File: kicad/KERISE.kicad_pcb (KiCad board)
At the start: 2 copper layers, 49 x 50 mm, 128 parts, among them J1 COM, J10 Ref_Slave, J11 Ref_Host, J12 Ref_Slave, J13 Ref_Host, J14 Ref_Slave, J15 Motor_L, J16 Motor_R, J17 5077CR-16-SMC2-BK-TR, J18 COM, J19 Charge1, J2 ENC_Host, J20 Charge2, J3 ENC_Slave, J4 ENC_Host, J5 ENC_Slave, J6 Fan, J7 Ref_Host, J8 Ref_Slave, J9 Ref_Host, P1 ToF_Host, P2 ToF_Slave, Q1 DMN3065LW-7, Q10 DMN3065LW-7, Q11 BSS138, Q12 BSS138, Q2 DMN3065LW-7, Q3 APDA3020P3C-P22, Q4 DMN3065LW-7, Q5 APDA3020P3C-P22, Q6 DMN3065LW-7, Q7 APDA3020P3C-P22, Q8 DMN3065LW-7, Q9 APDA3020P3C-P22, SW3 ENABLE, SW4 BOOT, U1 ESP32-PICO-V3-02, U10 NJM2863F33, U11 CH340K, U12 MCP73831-2-OT, U13 MCP73831-2-OT, U14 MCP73831-2-OT, U2 MA730, U3 MA730, U4 ICM-20600, U5 ICM-20600, U6 DRV8835, U7 LXDC2URxx, U8 VL6180X, U9 PCA9632

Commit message: 自動配線完了
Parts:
- moved R1 25.3 mm to (157.0, 124.0)
- moved R11 7.35 mm to (139.5, 124.3), turned to 90 degrees
- moved C20 6.49 mm to (140.5, 124.3), turned to -90 degrees
- moved R12 5.84 mm to (141.5, 124.3), turned to -90 degrees
- moved L1 1.76 mm to (140.0, 121.0), turned to 0 degrees
- moved L2 1.76 mm to (157.0, 121.0), turned to 180 degrees
- moved C17 0.25 mm to (154.2, 115.5)
- moved C18 0.25 mm to (154.8, 118.0)
- moved C19 0.25 mm to (156.0, 114.5)
- moved U6 0.25 mm to (157.2, 116.8)
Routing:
- net /Motor/MT_OUT_L2: track 0.00 -> 24.6 mm, vias 0 -> 1
- net /Motor/MT_OUT_L_L: track 0.00 -> 16.0 mm, vias 0 -> 2
- net /Motor/MT_OUT_L1: track 0.00 -> 5.58 mm
- net GND: track 51.5 -> 56.3 mm
- net /Motor/MT_OUT_R2: track 0.00 -> 4.71 mm
- net /Motor/MT_OUT_L_R: track 0.00 -> 4.61 mm
- net /Motor/MT_OUT_R1: track 0.00 -> 4.58 mm
- net +BATT: track 40.6 -> 43.2 mm

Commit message: とりあえず配線完了
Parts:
- added G***: LOGO, mouse:KERI_9mm, B.Cu at (148.5, 123.5)
- moved C20 0.72 mm to (141.2, 124.3)
- moved R11 0.72 mm to (140.2, 124.3)
- moved R12 0.72 mm to (142.2, 124.3)
- moved C27 0.32 mm to (143.3, 136.5)
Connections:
- net Net-(F1-Pad1) renamed /Flash/VBUS_FUSE
- SW3 pad 1: unconnected-(SW3-A-Pad1) -> /Flash/GND
- SW3 pad 3: /Flash/GND -> unconnected-(SW3-C-Pad3)
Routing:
- net +3.3V: track 7.25 -> 162.1 mm, vias 0 -> 3
- net GND: track 56.3 -> 200.6 mm, vias 0 -> 2
- net /Flash/GND: track 0.00 -> 118.4 mm
- net PR-LED-FL: track 0.00 -> 77.4 mm, vias 0 -> 2
- net ENABLE: track 0.00 -> 76.3 mm, vias 0 -> 4
- net SPI-MOSI: track 0.00 -> 73.5 mm, vias 0 -> 5
- net PR-RCV-FR: track 0.00 -> 70.8 mm, vias 0 -> 2
- net SPI-SCLK: track 0.00 -> 62.1 mm, vias 0 -> 5
- net +BATT: track 43.2 -> 104.4 mm, vias 2 -> 5
- net PR-LED-SL: track 0.00 -> 60.8 mm, vias 0 -> 2
- net PR-RCV-SR: track 0.00 -> 60.5 mm, vias 0 -> 4
- net SPI-MISO: track 0.00 -> 59.2 mm, vias 0 -> 4
- net SPEAKER: track 0.00 -> 55.2 mm, vias 0 -> 2
- net PR-LED-SR: track 0.00 -> 53.3 mm, vias 0 -> 2
- net /Flash/VBUS: track 0.00 -> 49.7 mm, vias 0 -> 7
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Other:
- board text added: "2023.11.23"
- board text added: "KERI's Lab 2023.11.23"
- board text removed: "2023.08.01"

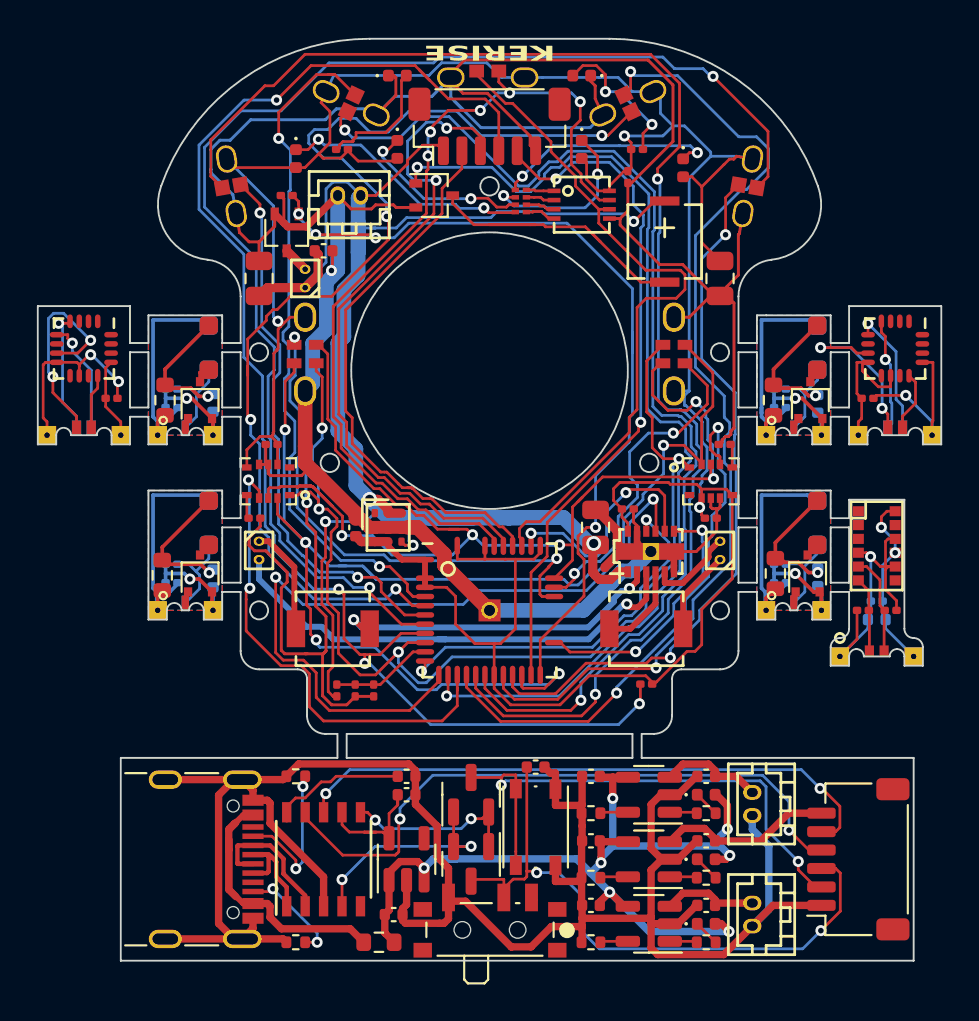
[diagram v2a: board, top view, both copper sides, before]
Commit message: Elecrowの指摘を修正
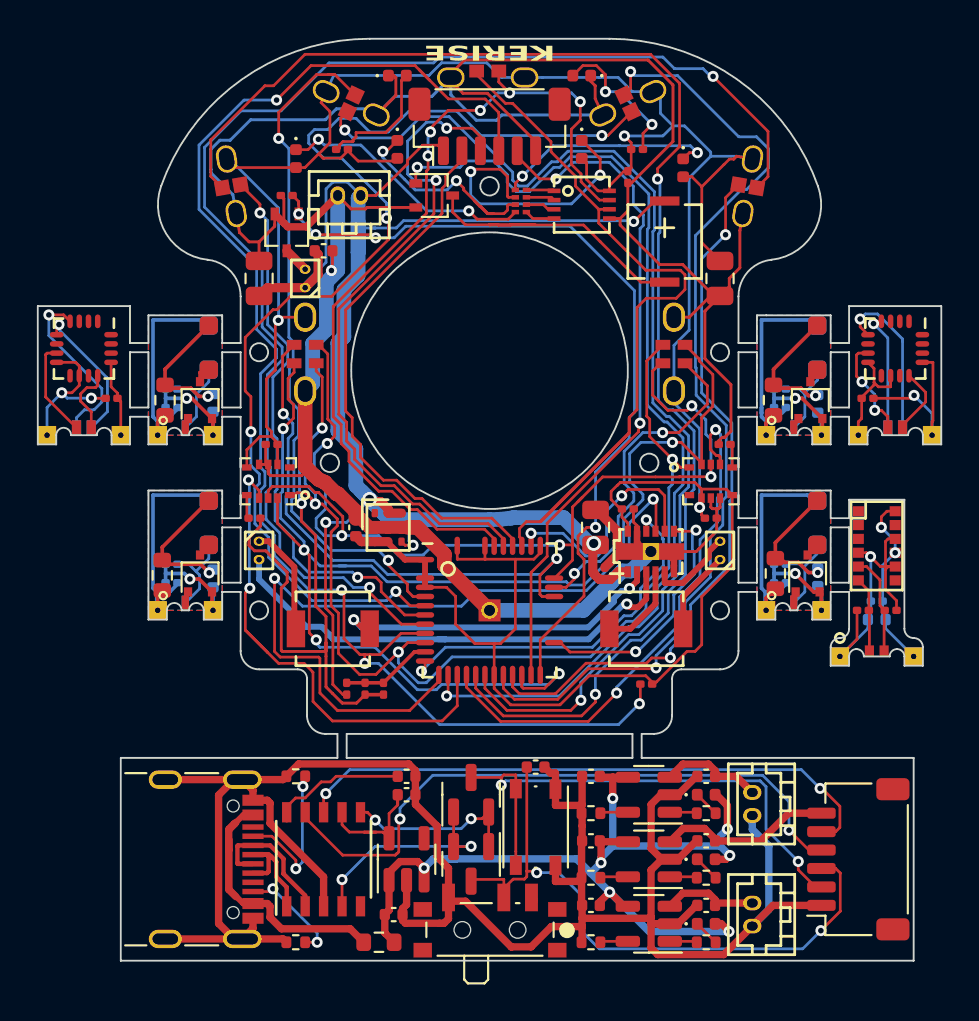
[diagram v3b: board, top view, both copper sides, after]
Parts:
- moved C20 0.54 mm to (141.8, 124.2)
- moved R11 0.54 mm to (140.8, 124.2)
- moved R12 0.54 mm to (142.8, 124.2)
- turned C2 to 180 degrees
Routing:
- net +BATT: track 104.4 -> 94.1 mm
- net I2C-SCL: track 37.5 -> 45.1 mm
- net SPI-SCLK: track 62.1 -> 55.0 mm
- net /Encoder_L/s_MISO: track 11.7 -> 5.30 mm, vias 2 -> 0
- net Net-(D8-K): track 9.66 -> 15.2 mm
- net /Encoder_R/s_MISO: track 9.50 -> 5.53 mm
- net /Encoder_L/s_MOSI: track 6.73 -> 9.59 mm
- net Net-(D9-K): track 9.75 -> 11.9 mm
- net /Encoder_L/s_GND: track 10.5 -> 8.61 mm
- net /Encoder_R/s_CS: track 7.03 -> 8.82 mm
- net /Encoder_R/s_GND: track 7.68 -> 6.03 mm
- net SPI-CS-IMU-L: track 26.1 -> 27.7 mm
- net /Encoder_L/s_CS: track 6.18 -> 7.65 mm
- net SPI-MOSI: track 73.5 -> 74.8 mm
- net ENABLE: track 76.3 -> 77.5 mm
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
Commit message: 1回目の基板修正
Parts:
- removed the C29 at (151.0, 128.5)
- removed Q11, Q12: BSS138, Package_TO_SOT_SMD:SOT-23
- removed the U11 at (139.5, 133.5)
- added SW1: RESET, mouse:EVPBB, F.Cu at (136.0, 92.5)
- added SW2: UPLOAD, mouse:EVPBB, F.Cu at (161.0, 92.5)
- added U10: FT234XD, Package_DFN_QFN:DFN-12-1EP_3x3mm_P0.5mm_EP1.6x2.5mm, F.Cu at (141.8, 131.5)
- C10, C11, C12, C13, C15, C9, J3, J5, Q3, Q5, Q7, Q9, R10, R8: moved to F.Cu
- D1, D2, D3, D4, J12, J14, Q2, Q4, Q6, Q8: moved to B.Cu
- R19, R20, R21: value 4.7k -> 1k
- R3, R5, R7, R9: footprint Resistor_SMD:R_0603_1608Metric -> Resistor_SMD:R_0402_1005Metric
- SW3: value ENABLE -> RESET; footprint Button_Switch_SMD:SW_SPDT_PCM12 -> Button_Switch_SMD:SW_Push_1P1T_NO_Vertical_Wuerth_434133025816
- moved D4 12.5 mm to (125.7, 105.2)
- moved Q9 12.5 mm to (125.7, 105.2)
- moved C15 12.4 mm to (125.5, 108.8)
- moved Q8 11.8 mm to (126.2, 108.2)
- moved J3 11.2 mm to (131.5, 120.5), turned to 0 degrees
- moved D1 11.2 mm to (171.3, 105.2), turned to -90 degrees
- moved J5 11.2 mm to (165.5, 120.5), turned to 0 degrees
- moved Q3 11.2 mm to (171.3, 105.2), turned to 90 degrees
- moved U2 11.2 mm to (131.5, 115.8), turned to 0 degrees
- moved U3 11.2 mm to (165.5, 115.8), turned to 0 degrees
- moved C2 11.1 mm to (133.0, 118.4)
- moved C10 11.0 mm to (169.8, 109.0), turned to 0 degrees
- moved Q2 11.0 mm to (170.8, 108.2)
- moved C9 10.8 mm to (171.5, 108.8)
- moved J14 10.7 mm to (127.0, 110.5), turned to 180 degrees
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- renumbered C30 to C29, C31 to C30, C32 to C31, C33 to C32, C34 to C33, C35 to C34, J18 to J17, J17 to J18, U10 to U11
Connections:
- C26 pad 2: Net-(U11-V3) -> /Flash/VCC
- SW3 pad 1: /Flash/GND -> /Flash/ESP32_EN
- SW3 pad 2: /Flash/ESP32_EN -> /Flash/GND
- U11 pad 4: unconnected-(U10-BYP-Pad4) -> (no net)
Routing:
- net /Flash/GND: track 118.4 -> 98.5 mm, vias 0 -> 1
- net GND: track 199.9 -> 217.0 mm, vias 2 -> 1
- net /Encoder_L/s_VDD: track 4.17 -> 18.4 mm, vias 0 -> 1
- net /Flash/ESP32_RX: track 32.5 -> 18.6 mm
- net /Flash/ESP32_EN: track 34.5 -> 22.1 mm
- net /Flash/RTS: track 12.0 -> 0.00 mm, vias 2 -> 0
- net /Flash/ESP32_TX: track 34.9 -> 23.2 mm
- net /Flash/DTR: track 9.57 -> 0.00 mm, vias 2 -> 0
- net BUTTON: track 37.6 -> 46.8 mm, vias 2 -> 3
- net /Encoder_R/s_VDD: track 9.37 -> 18.5 mm
- net /Flash/ESP32_BT: track 29.3 -> 21.0 mm, vias 2 -> 3
- net /Flash/VBUS_FUSE: track 18.1 -> 10.4 mm
- net Net-(U11-V3): track 7.49 -> 0.00 mm
- net I2C-SCL: track 45.1 -> 38.2 mm
- net /Flash/VBUS: track 49.7 -> 42.9 mm, vias 7 -> 6
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- added copper zone on B.Cu, net /Flash/GND
- added copper zone on F.Cu, net /Flash/GND
- added copper zone on B.Cu, net /IR_RCV_FL/LED_to_FET
- added copper zone on F.Cu, net /IR_RCV_FL/s_IR_RCV
- added copper zone on B.Cu, net /IR_RCV_FR/LED_to_FET
- added copper zone on F.Cu, net /IR_RCV_FR/s_IR_RCV
- added copper zone on B.Cu, net /IR_RCV_SL/LED_to_C
- added copper zone on F.Cu, net /IR_RCV_SL/s_3.3V
- added copper zone on B.Cu, net /IR_RCV_SR/LED_to_C
- added copper zone on F.Cu, net /IR_RCV_SR/s_3.3V
- removed copper zone on F.Cu, net /IR_RCV_FL/LED_to_C
- removed copper zone on B.Cu, net /IR_RCV_FL/s_IR_RCV
- removed copper zone on F.Cu, net /IR_RCV_FR/LED_to_C
- removed copper zone on B.Cu, net /IR_RCV_FR/s_IR_RCV
- removed copper zone on F.Cu, net /IR_RCV_SL/LED_to_C
- removed copper zone on B.Cu, net /IR_RCV_SL/s_IR_RCV
- removed copper zone on F.Cu, net /IR_RCV_SR/LED_to_C
- removed copper zone on B.Cu, net /IR_RCV_SR/s_IR_RCV
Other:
- board size 49 x 50 mm -> 48 x 50 mm
- board text added: "B"
- board text added: "KERI's Lab 2023.12.27"
- board text added: "KERISE v6"
- board text added: "R"
- board text removed: "2023.11.23"
- board text removed: "KERI's Lab 2023.11.23"
- board text removed: "KERISE"
